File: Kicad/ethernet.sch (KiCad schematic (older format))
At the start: 27 parts, among them J301 RJ45_Amphenol_RJMG1BD3B8K1ANR, U301 ENC424J600-PT, Y301 25M

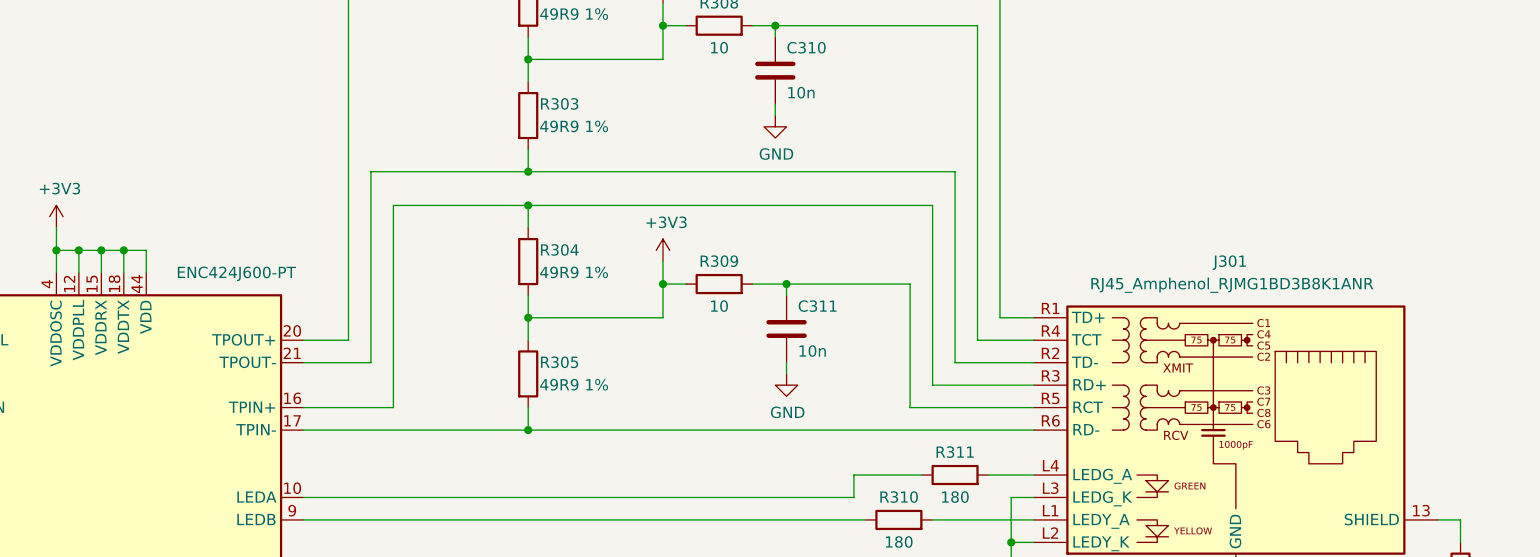
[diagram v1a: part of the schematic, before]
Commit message: Replaced NUC029 (TSSOP) with KE04 (SOIC).
Also updated the BOM with some part nos.
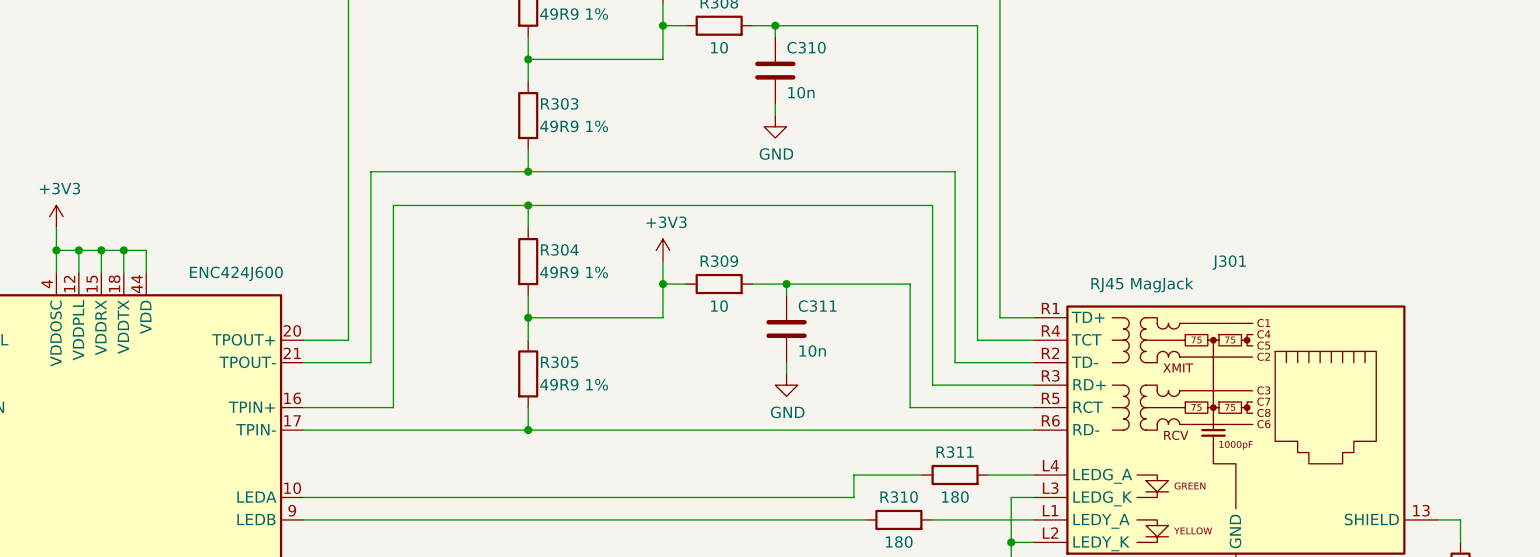
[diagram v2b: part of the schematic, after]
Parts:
- C301, C302, C303, C304, C305: Digikey (none) -> BC1150CT-ND; MPN (none) -> K104K15X7RF5TL2; Manufacturer (none) -> Vishay
- J301: value RJ45_Amphenol_RJMG1BD3B8K1ANR -> RJ45 MagJack; Digikey (none) -> RJMG1BD3B8K1ANR-ND; MPN (none) -> RJMG1BD3B8K1ANR; Manufacturer (none) -> Amphenol
- U301: value ENC424J600-PT -> ENC424J600; Digikey (none) -> ENC424J600-I/PT-ND; MPN (none) -> ENC424J600-I/PT; Manufacturer (none) -> Microchip
- Y301: Digikey (none) -> 535-9050-ND; MPN (none) -> ABL-25.000MHZ-B2F; Manufacturer (none) -> Abracon
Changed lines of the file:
@@
 P 9250 3700
 F 0 "J301" H 9150 4450 50  0000 L CNN
-F 1 "RJ45_Amphenol_RJMG1BD3B8K1ANR" H 8600 4350 50  0000 L CNN
+F 1 "RJ45 MagJack" H 8600 4350 50  0000 L CNN
 F 2 "Connector_RJ:RJ45_Amphenol_RJMG1BD3B8K1ANR" H 9250 4400 50  0001 C CNN
 F 3 "https://www.amphenolcanada.com/ProductSearch/Drawings/AC/RJMG1BD3B8K1ANR.PDF" H 9250 4500 50  0001 C CNN
 F 4 "0" H 9250 3700 50  0001 C CNN "DNP"
+F 5 "RJMG1BD3B8K1ANR-ND" H 9250 3700 50  0001 C CNN "Digikey"
+F 6 "RJMG1BD3B8K1ANR" H 9250 3700 50  0001 C CNN "MPN"
+F 7 "Amphenol" H 9250 3700 50  0001 C CNN "Manufacturer"
 	1    9250 3700
 	1    0    0    -1
@@
 P 4200 4400
 F 0 "U301" H 3500 5800 50  0000 C CNN
-F 1 "ENC424J600-PT" H 4800 5800 50  0000 C CNN
+F 1 "ENC424J600" H 4800 5800 50  0000 C CNN
 F 2 "Package_QFP:TQFP-44_10x10mm_P0.8mm" H 5250 3050 50  0001 C CNN
 F 3 "http://ww1.microchip.com/downloads/en/DeviceDoc/39935c.pdf" H 4250 5200 50  0001 C CNN
 F 4 "0" H 4200 4400 50  0001 C CNN "DNP"
+F 5 "ENC424J600-I/PT-ND" H 4200 4400 50  0001 C CNN "Digikey"
+F 6 "ENC424J600-I/PT" H 4200 4400 50  0001 C CNN "MPN"
+F 7 "Microchip" H 4200 4400 50  0001 C CNN "Manufacturer"
 	1    4200 4400
 	1    0    0    -1
@@
 F 3 "~" H 6700 5050 50  0001 C CNN
 F 4 "0" H 6700 5050 50  0001 C CNN "DNP"
+F 5 "535-9050-ND" H 6700 5050 50  0001 C CNN "Digikey"
+F 6 "ABL-25.000MHZ-B2F" H 6700 5050 50  0001 C CNN "MPN"
+F 7 "Abracon" H 6700 5050 50  0001 C CNN "Manufacturer"
 	1    6700 5050
 	1    0    0    -1
@@
 F 3 "~" H 2900 7250 50  0001 C CNN
 F 4 "0" H 2900 7250 50  0001 C CNN "DNP"
+F 5 "BC1150CT-ND" H 2900 7250 50  0001 C CNN "Digikey"
+F 6 "K104K15X7RF5TL2" H 2900 7250 50  0001 C CNN "MPN"
+F 7 "Vishay" H 2900 7250 50  0001 C CNN "Manufacturer"
 	1    2900 7250
 	1    0    0    -1
@@
 F 3 "~" H 2450 7250 50  0001 C CNN
 F 4 "0" H 2450 7250 50  0001 C CNN "DNP"
+F 5 "BC1150CT-ND" H 2450 7250 50  0001 C CNN "Digikey"
+F 6 "K104K15X7RF5TL2" H 2450 7250 50  0001 C CNN "MPN"
+F 7 "Vishay" H 2450 7250 50  0001 C CNN "Manufacturer"
 	1    2450 7250
 	1    0    0    -1
@@
 F 3 "~" H 2000 7250 50  0001 C CNN
 F 4 "0" H 2000 7250 50  0001 C CNN "DNP"
+F 5 "BC1150CT-ND" H 2000 7250 50  0001 C CNN "Digikey"
+F 6 "K104K15X7RF5TL2" H 2000 7250 50  0001 C CNN "MPN"
+F 7 "Vishay" H 2000 7250 50  0001 C CNN "Manufacturer"
 	1    2000 7250
 	1    0    0    -1
@@
 F 3 "~" H 1550 7250 50  0001 C CNN
 F 4 "0" H 1550 7250 50  0001 C CNN "DNP"
+F 5 "BC1150CT-ND" H 1550 7250 50  0001 C CNN "Digikey"
+F 6 "K104K15X7RF5TL2" H 1550 7250 50  0001 C CNN "MPN"
+F 7 "Vishay" H 1550 7250 50  0001 C CNN "Manufacturer"
 	1    1550 7250
 	1    0    0    -1
@@
 F 3 "~" H 1100 7250 50  0001 C CNN
 F 4 "0" H 1100 7250 50  0001 C CNN "DNP"
+F 5 "BC1150CT-ND" H 1100 7250 50  0001 C CNN "Digikey"
+F 6 "K104K15X7RF5TL2" H 1100 7250 50  0001 C CNN "MPN"
+F 7 "Vishay" H 1100 7250 50  0001 C CNN "Manufacturer"
 	1    1100 7250
 	1    0    0    -1

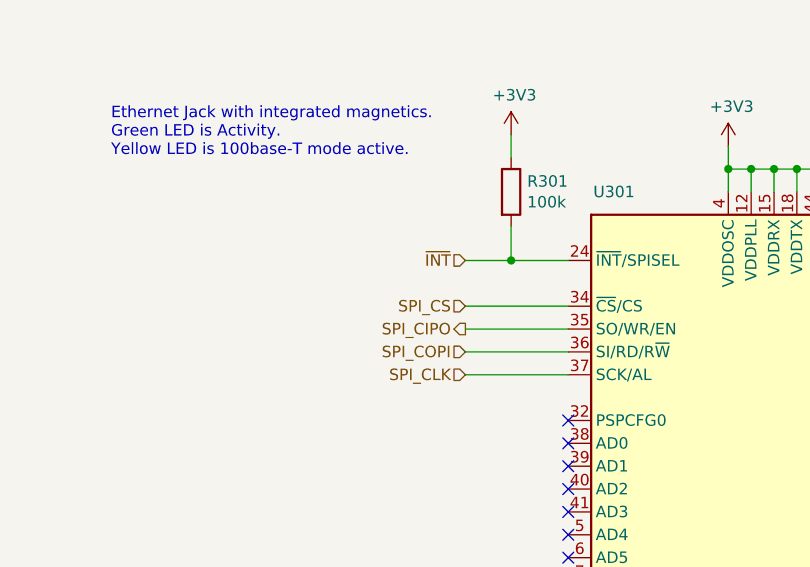
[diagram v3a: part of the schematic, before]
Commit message: Revised CPU connector to be two 2x20.
This gives more room for larger TQFP-176+ CPUs to be fitted that
didn't fit on the PGA-80 design.
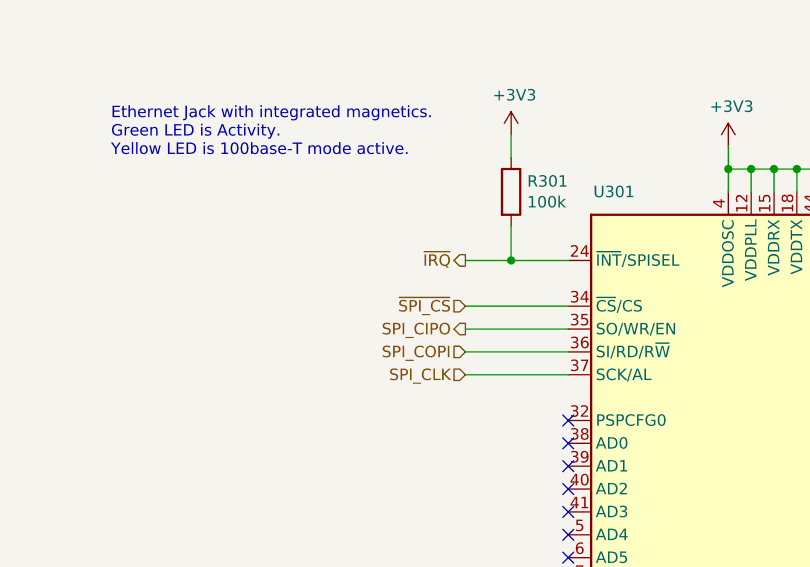
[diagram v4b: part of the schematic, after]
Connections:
- net SPI_CS renamed ~SPI_CS
- net ~INT renamed ~IRQ
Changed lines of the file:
@@
 $Descr A4 11693 8268
 encoding utf-8
-Sheet 3 8
+Sheet 8 8
 Title "Neotron Common Hardware - Ethernet MAC/PHY"
 Date "2020-12-26"
@@
 SPI_CIPO
 Text HLabel 2850 3500 0    50   Input ~ 0
-SPI_CS
+~SPI_CS
 Text HLabel 2850 3800 0    50   Input ~ 0
 SPI_CLK
@@
 	1    0    0    -1
 $EndComp
-Text HLabel 2850 3300 0    50   Input ~ 0
-~INT
+Text HLabel 2850 3300 0    50   Output ~ 0
+~IRQ
 $Comp
 L Device:Crystal Y301

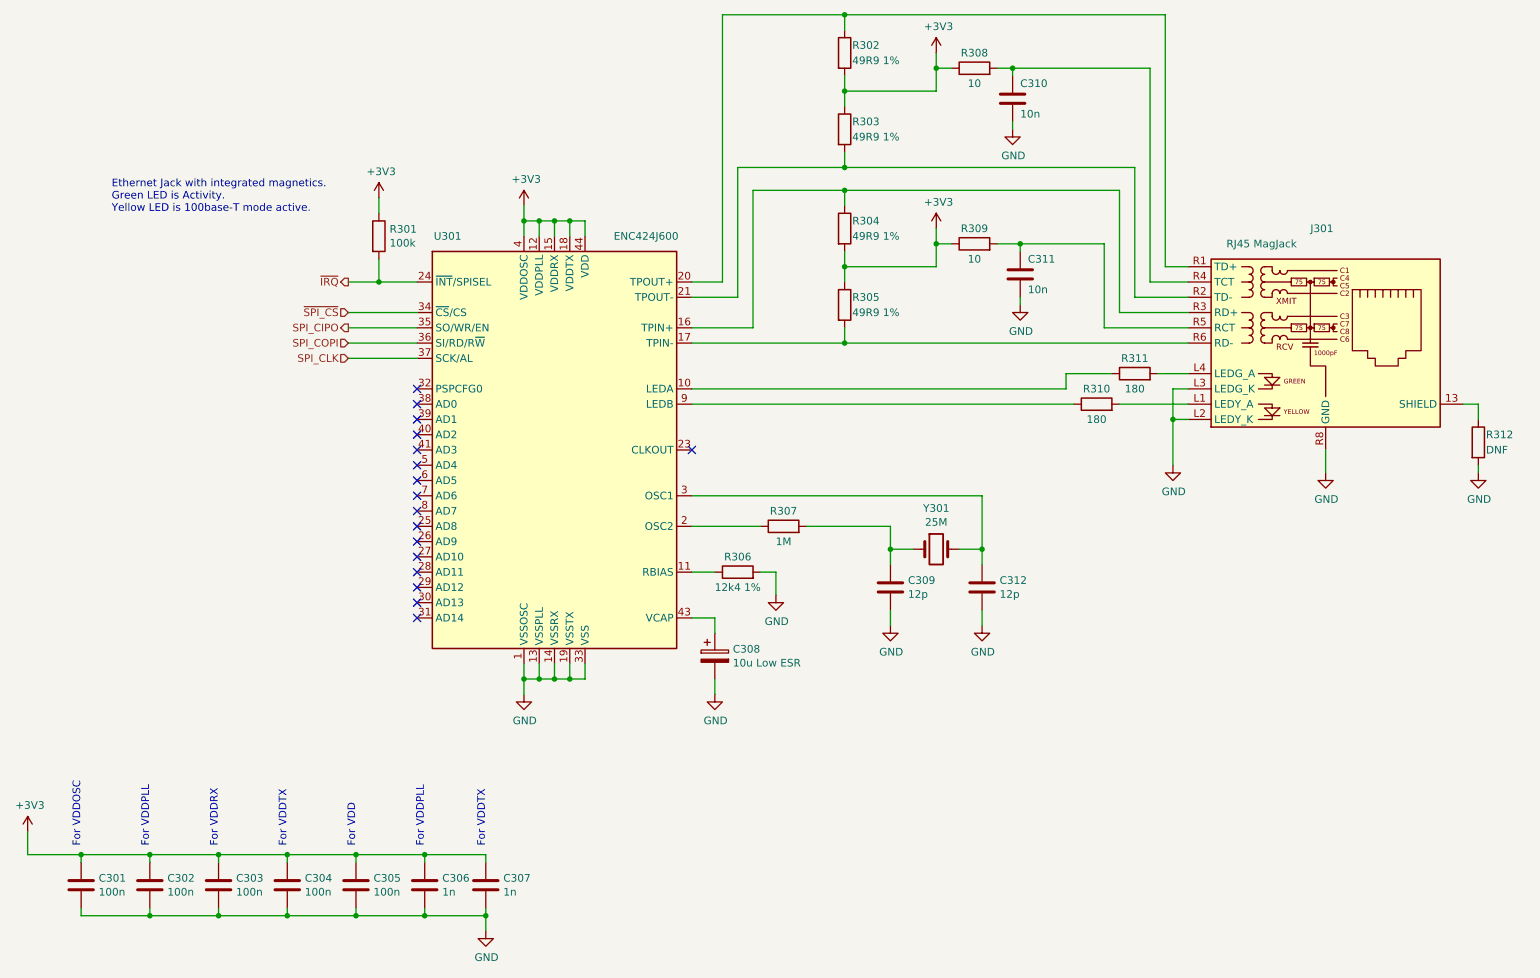
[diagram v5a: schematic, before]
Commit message: Bring in R2R DAC from Neotron-9X schematic.
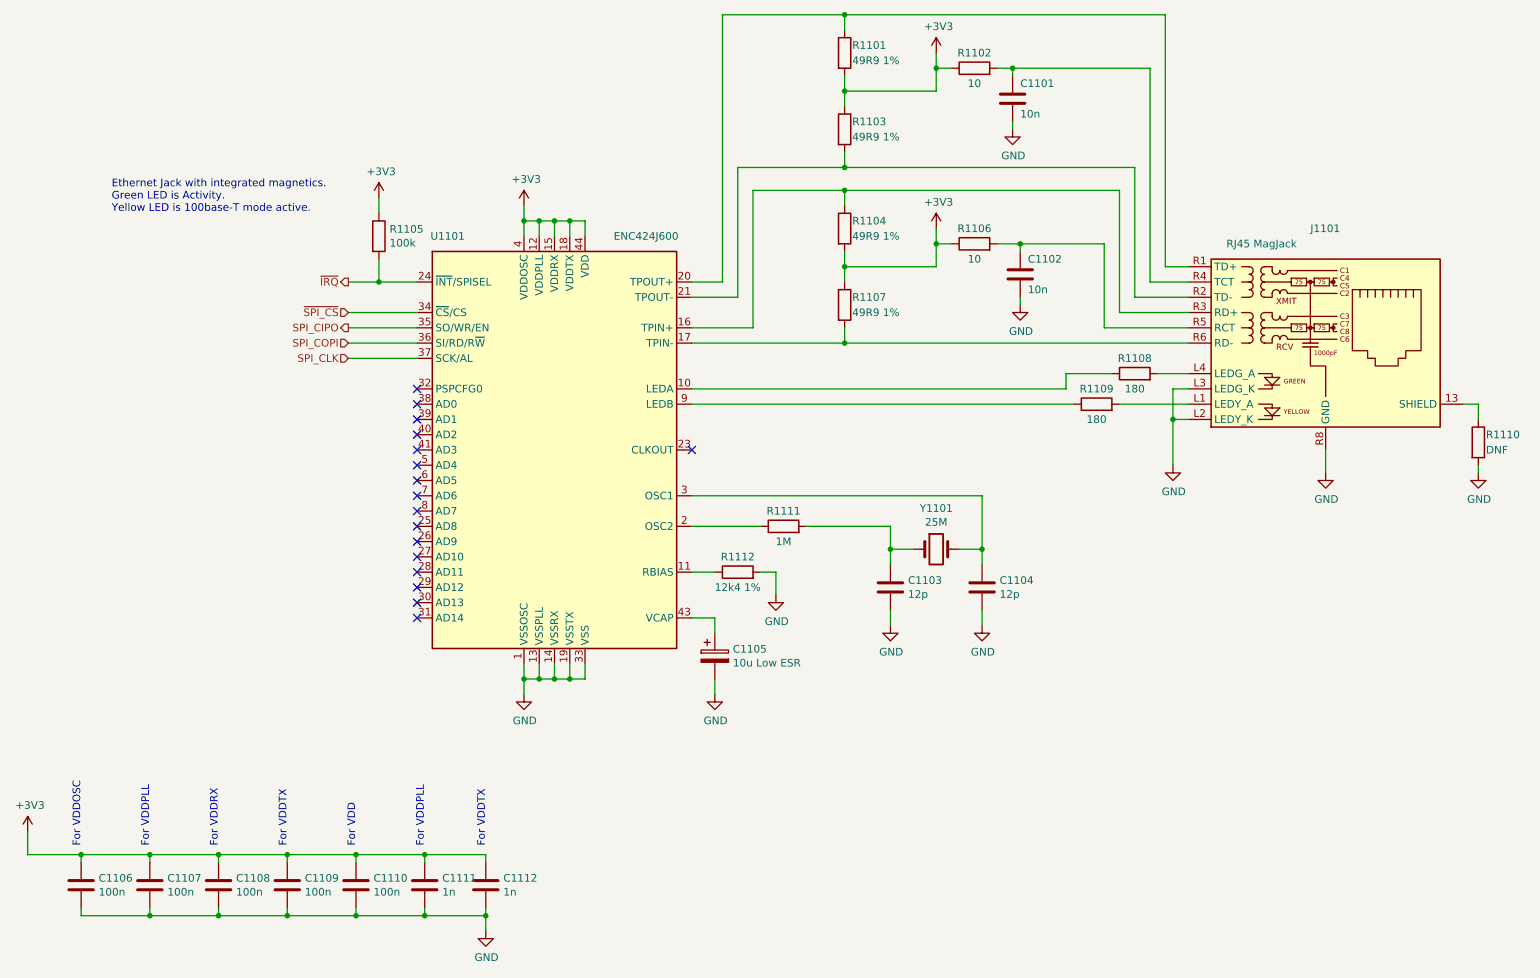
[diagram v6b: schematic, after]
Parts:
- renumbered C310 to C1101, C311 to C1102, C309 to C1103, C312 to C1104, C308 to C1105, C301 to C1106, C302 to C1107, C303 to C1108, C304 to C1109, C305 to C1110, C306 to C1111, C307 to C1112, J301 to J1101, R302 to R1101, R308 to R1102, R303 to R1103, R304 to R1104, R301 to R1105, R309 to R1106, R305 to R1107, R311 to R1108, R310 to R1109, R312 to R1110, R307 to R1111, R306 to R1112, U301 to U1101, Y301 to Y1101
